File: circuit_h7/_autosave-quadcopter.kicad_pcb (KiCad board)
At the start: 4 copper layers, 37.5 x 37.5 mm, 108 parts, among them J1 Conn_01x04_Male, J10 Conn_01x01_Female, J11 Conn_01x04_Male, J12 Conn_01x04_Male, J13 Conn_01x01_Female, J14 Conn_01x01_Female, J16 Conn_01x01_Female, J17 Conn_01x01_Female, J18 USB_C_Receptacle_USB2.0, J19 Conn_01x08_Male, J2 Conn_01x01_Female, J21 Conn_01x01_Female, J22 Conn_01x01_Female, J23 Conn_01x01_Female, J24 Conn_01x01_Female, J25 Conn_01x01_Female, J26 Conn_01x01_Female, J28 Conn_01x01_Female, J29 Conn_01x01_Female, J3 Conn_01x01_Female, J30 Conn_01x01_Female, J31 Conn_01x01_Female, J32 Conn_01x01_Female, J33 Conn_01x01_Female, J37 Conn_01x01_Female, J4 Conn_01x01_Female, J40 Conn_01x01_Female, J41 Conn_01x01_Female, J42 Conn_01x01_Female, J43 Conn_01x01_Female, J44 Conn_01x01_Female, J45 Conn_01x01_Female, J47 Conn_01x01_Female, J48 Conn_01x01_Female, J49 Conn_01x01_Female, J5 Conn_Coaxial, J50 Conn_01x01_Female, J6 Conn_01x06_Male, J7 Conn_01x01_Female, J8 Conn_01x01_Female, J9 Conn_01x01_Female, SW1 SW_DIP_x01, U1 STM32H723VGH6, U2 ICM-42605, U3 DPS310, U4 3V3, U5 EUP3458 1.2A, 30V max input, 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, U6 2450FM07D0034T, U7 W25Q80DVUXIE TR (16M), U8 SX1281, U9 5v, 500mA, Y1 16M, Y2 52Mhz, 12pF

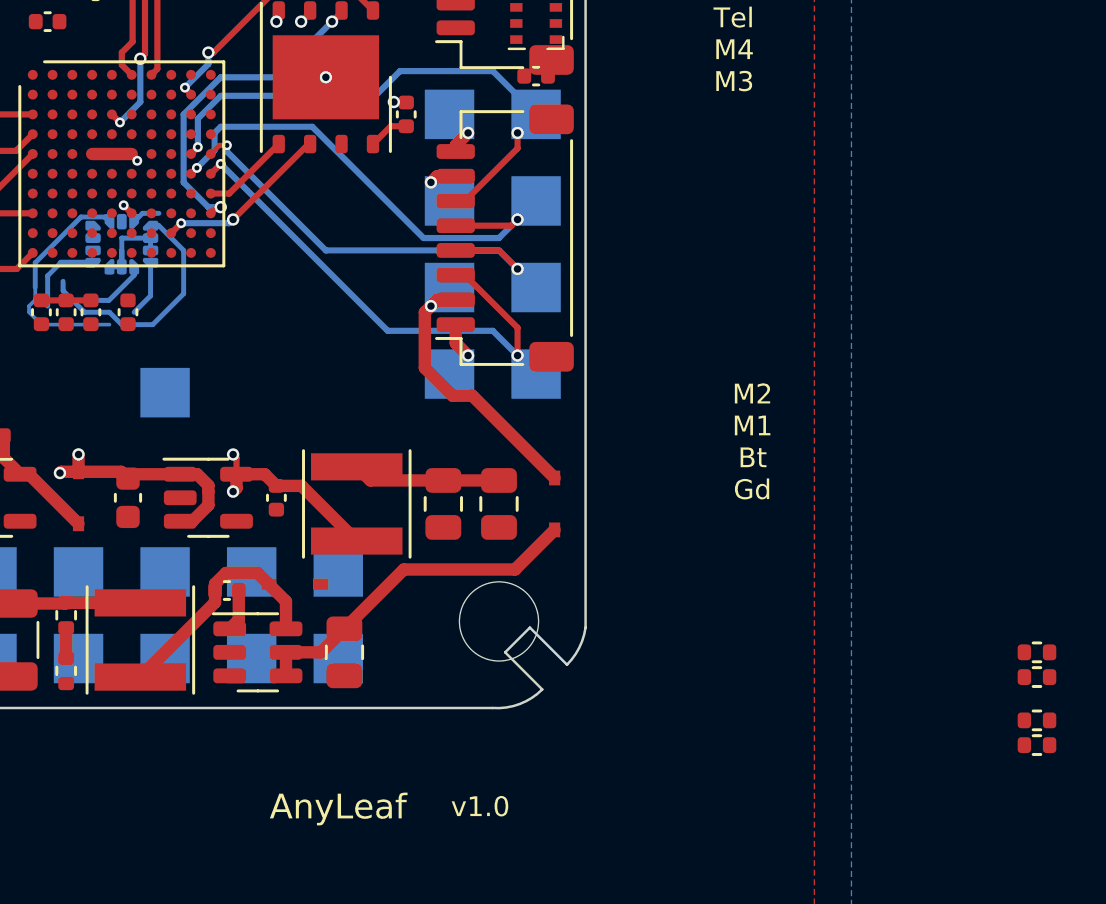
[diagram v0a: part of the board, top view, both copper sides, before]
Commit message: Started work on getting all 4 motors on same timer for H7 design
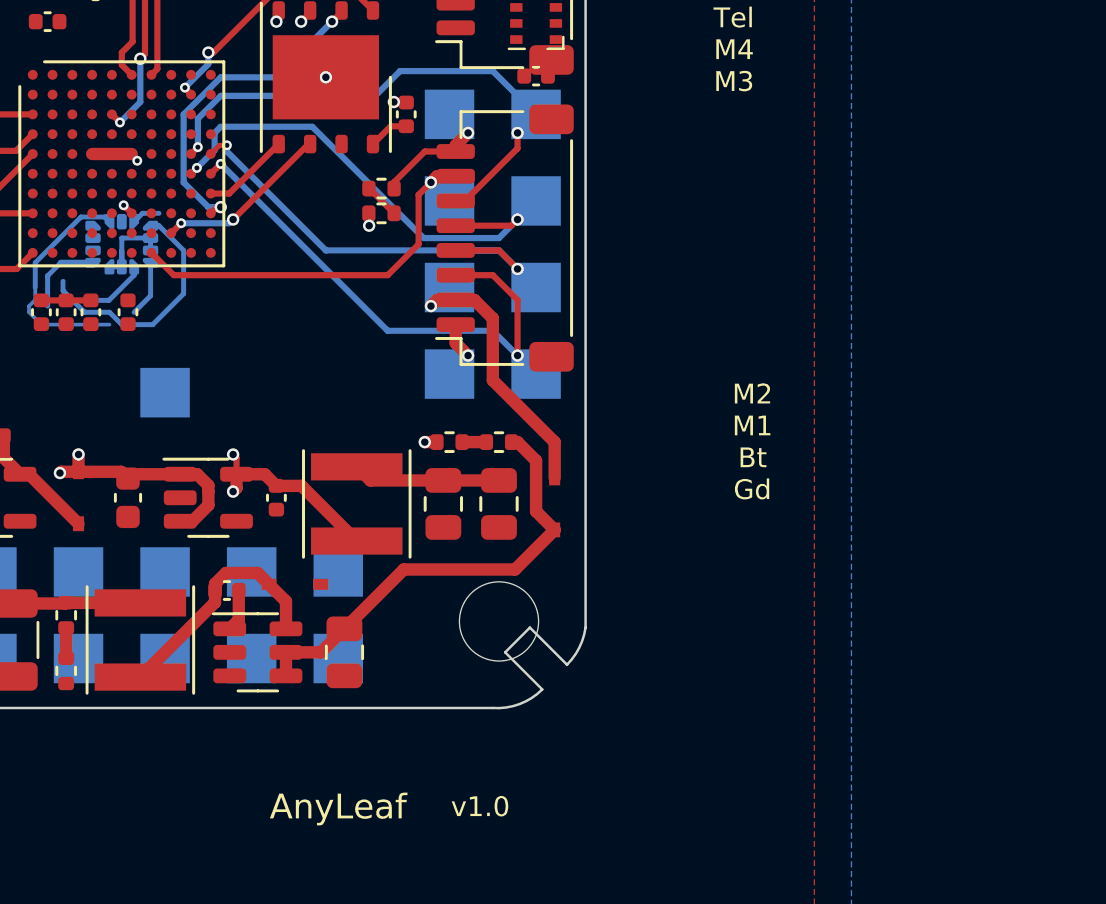
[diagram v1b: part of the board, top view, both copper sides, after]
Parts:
- moved R16 34.8 mm to (147.5, 85.2)
- moved R18 33.5 mm to (147.5, 86.2)
- moved R14 25.2 mm to (150.2, 95.5)
- moved R13 23.7 mm to (152.2, 95.5), turned to 0 degrees
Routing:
- net /UART3_RX: track 1.10 -> 15.5 mm
- net +BATT: track 13.9 -> 18.3 mm
- net /CURRENT: track 1.71 -> 4.97 mm
- net /CUR_DIV: track 0.00 -> 1.43 mm
- net GND: track 17.7 -> 18.6 mm, vias 8 -> 10
- net /BATT_DIV: track 0.00 -> 0.98 mm
- net /M1: track 20.3 -> 20.9 mm
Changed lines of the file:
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@@
   )
   (footprint "Resistor_SMD:R_0402_1005Metric" (layer "F.Cu")
-    (at 174 104)
+    (at 150.25 95.5)
     (descr "Resistor SMD 0402 (1005 Metric), square (rectangular) end terminal, IPC_7351 nominal, (Body size source: IPC-SM-782 page 72, https://www.pcb-3d.com/wordpress/wp-content/uploads/ipc-sm-782a_amendment_1_and_2.pdf), generated with kicad-footprint-generator")
     (tags "resistor")
@@
   )
   (footprint "Resistor_SMD:R_0402_1005Metric" (layer "F.Cu")
-    (at 174 107.75)
+    (at 147.5 85.25)
     (descr "Resistor SMD 0402 (1005 Metric), square (rectangular) end terminal, IPC_7351 nominal, (Body size source: IPC-SM-782 page 72, https://www.pcb-3d.com/wordpress/wp-content/uploads/ipc-sm-782a_amendment_1_and_2.pdf), generated with kicad-footprint-generator")
     (tags "resistor")
@@
   )
   (footprint "Resistor_SMD:R_0402_1005Metric" (layer "F.Cu")
-    (at 174 105 180)
+    (at 152.25 95.5)
     (descr "Resistor SMD 0402 (1005 Metric), square (rectangular) end terminal, IPC_7351 nominal, (Body size source: IPC-SM-782 page 72, https://www.pcb-3d.com/wordpress/wp-content/uploads/ipc-sm-782a_amendment_1_and_2.pdf), generated with kicad-footprint-generator")
     (tags "resistor")
@@
     (fp_line (start 0.525 -0.27) (end 0.525 0.27) (layer "F.Fab") (width 0.1))
     (fp_line (start -0.525 -0.27) (end 0.525 -0.27) (layer "F.Fab") (width 0.1))
-    (pad "1" smd roundrect locked (at -0.51 0 180) (size 0.54 0.64) (layers "F.Cu" "F.Paste" "F.Mask") (roundrect_rratio 0.25)
+    (pad "1" smd roundrect locked (at -0.51 0) (size 0.54 0.64) (layers "F.Cu" "F.Paste" "F.Mask") (roundrect_rratio 0.25)
       (net 57 "/BATT_DIV") (pintype "passive"))
-    (pad "2" smd roundrect locked (at 0.51 0 180) (size 0.54 0.64) (layers "F.Cu" "F.Paste" "F.Mask") (roundrect_rratio 0.25)
+    (pad "2" smd roundrect locked (at 0.51 0) (size 0.54 0.64) (layers "F.Cu" "F.Paste" "F.Mask") (roundrect_rratio 0.25)
       (net 15 "+BATT") (pintype "passive"))
     (model "${KICAD6_3DMODEL_DIR}/Resistor_SMD.3dshapes/R_0402_1005Metric.wrl"
@@
   )
   (footprint "Resistor_SMD:R_0402_1005Metric" (layer "F.Cu")
-    (at 174 106.75)
+    (at 147.5 86.25)
     (descr "Resistor SMD 0402 (1005 Metric), square (rectangular) end terminal, IPC_7351 nominal, (Body size source: IPC-SM-782 page 72, https://www.pcb-3d.com/wordpress/wp-content/uploads/ipc-sm-782a_amendment_1_and_2.pdf), generated with kicad-footprint-generator")
     (tags "resistor")
@@
   (segment (start 148.02 81.77) (end 148 81.75) (width 0.25) (layer "F.Cu") (net 8))
   (segment (start 122.75 82.25) (end 123.5 83) (width 0.25) (layer "F.Cu") (net 8))
+  (segment (start 146.99 86.74) (end 147 86.75) (width 0.25) (layer "F.Cu") (net 8))
   (segment (start 123.5 83) (end 123.5 83.5) (width 0.25) (layer "F.Cu") (net 8))
   (segment (start 122.075 82.25) (end 122.75 82.25) (width 0.25) (layer "F.Cu") (net 8))
+  (segment (start 146.99 86.25) (end 146.99 86.74) (width 0.25) (layer "F.Cu") (net 8))
+  (segment (start 149.74 95.5) (end 149.25 95.5) (width 0.5) (layer "F.Cu") (net 8))
   (segment (start 137.1875 72.75) (end 137.0525 72.885) (width 0.2) (layer "F.Cu") (net 8))
   (segment (start 139.125 74) (end 139.125 74.5) (width 0.25) (layer "F.Cu") (net 8))
@@
   (via (at 145.25 80.75) (size 0.5) (drill 0.3) (layers "F.Cu" "B.Cu") (net 8))
   (via (at 137.625 84.125) (size 0.4) (drill 0.2) (layers "F.Cu" "B.Cu") (net 8))
+  (via (at 147 86.75) (size 0.5) (drill 0.3) (layers "F.Cu" "B.Cu") (net 8))
   (via (at 143.25 78.5) (size 0.5) (drill 0.3) (layers "F.Cu" "B.Cu") (net 8))
   (via (at 137.25 73.75) (size 0.5) (drill 0.3) (layers "F.Cu" "B.Cu") (net 8))
@@
   (via (at 148 81.75) (size 0.5) (drill 0.3) (layers "F.Cu" "B.Cu") (net 8))
   (via (at 123.5 83.5) (size 0.5) (drill 0.3) (layers "F.Cu" "B.Cu") (net 8))
+  (via (at 149.25 95.5) (size 0.5) (drill 0.3) (layers "F.Cu" "B.Cu") (net 8))
   (segment (start 137 88.4125) (end 136.5 88.4125) (width 0.2) (layer "B.Cu") (net 8))
   (segment (start 137 87.75) (end 137 88.4125) (width 0.2) (layer "B.Cu") (net 8))
@@
   (segment (start 135.439438 100.689438) (end 135.25 100.5) (width 0.25) (layer "B.Cu") (net 14))
   (segment (start 152.899521 100.650479) (end 154.5 99.05) (width 0.5) (layer "F.Cu") (net 15))
+  (segment (start 153.75 96.25) (end 153.75 98.3) (width 0.5) (layer "F.Cu") (net 15))
+  (segment (start 152.76 95.5) (end 153 95.5) (width 0.5) (layer "F.Cu") (net 15))
+  (segment (start 153.75 98.3) (end 154.5 99.05) (width 0.5) (layer "F.Cu") (net 15))
   (segment (start 148.399521 100.650479) (end 152.899521 100.650479) (width 0.5) (layer "F.Cu") (net 15))
   (segment (start 146 103.05) (end 145.05 104) (width 0.5) (layer "F.Cu") (net 15))
   (segment (start 145.05 104) (end 143.6375 104) (width 0.5) (layer "F.Cu") (net 15))
+  (segment (start 153 95.5) (end 153.75 96.25) (width 0.5) (layer "F.Cu") (net 15))
   (segment (start 143.6375 104) (end 143.6375 104.95) (width 0.5) (layer "F.Cu") (net 15))
   (segment (start 146 103.05) (end 148.399521 100.650479) (width 0.5) (layer "F.Cu") (net 15))
@@
   (segment (start 132.725489 83.724511) (end 130.474511 83.724511) (width 0.25) (layer "F.Cu") (net 22))
   (segment (start 150.5 83.75) (end 150.5 83.5) (width 0.5) (layer "F.Cu") (net 23))
+  (segment (start 149.25 83.75) (end 148.01 84.99) (width 0.25) (layer "F.Cu") (net 23))
   (segment (start 150.5 83.5) (end 151 83) (width 0.5) (layer "F.Cu") (net 23))
+  (segment (start 148.01 84.99) (end 148.01 85.25) (width 0.25) (layer "F.Cu") (net 23))
+  (segment (start 150.5 83.75) (end 149.25 83.75) (width 0.25) (layer "F.Cu") (net 23))
   (via (at 151 83) (size 0.5) (drill 0.3) (layers "F.Cu" "B.Cu") (net 23))
   (segment (start 150 82.25) (end 150 83) (width 0.2) (layer "B.Cu") (net 23))
-  (segment (start 151.175 93.625) (end 150.375 93.625) (width 0.5) (layer "F.Cu") (net 26))
-  (segment (start 149.25 90.25) (end 149.25 92.5) (width 0.5) (layer "F.Cu") (net 26))
-  (segment (start 149.5 90) (end 149.25 90.25) (width 0.5) (layer "F.Cu") (net 26))
-  (segment (start 149.25 92.5) (end 150.375 93.625) (width 0.5) (layer "F.Cu") (net 26))
+  (segment (start 154.5 95.5) (end 152 93) (width 0.5) (layer "F.Cu") (net 26))
+  (segment (start 152 90.5) (end 151.25 89.75) (width 0.5) (layer "F.Cu") (net 26))
+  (segment (start 152 93) (end 152 90.5) (width 0.5) (layer "F.Cu") (net 26))
   (segment (start 150.5 89.75) (end 149.75 89.75) (width 0.5) (layer "F.Cu") (net 26))
-  (segment (start 154.5 96.95) (end 151.175 93.625) (width 0.5) (layer "F.Cu") (net 26))
+  (segment (start 154.5 96.95) (end 154.5 95.5) (width 0.5) (layer "F.Cu") (net 26))
+  (segment (start 151.25 89.75) (end 150.5 89.75) (width 0.5) (layer "F.Cu") (net 26))
   (segment (start 149.75 89.75) (end 149.5 90) (width 0.5) (layer "F.Cu") (net 26))
   (via (at 149.5 90) (size 0.5) (drill 0.3) (layers "F.Cu" "B.Cu") (net 26))
@@
   (via (at 120.75 81.5) (size 0.5) (drill 0.3) (layers "F.Cu" "B.Cu") (net 32))
   (segment (start 150.5 84.75) (end 149.75 84.75) (width 0.5) (layer "F.Cu") (net 34))
+  (segment (start 149 87.5) (end 149 85.5) (width 0.25) (layer "F.Cu") (net 34))
   (segment (start 149.75 84.75) (end 149.5 85) (width 0.5) (layer "F.Cu") (net 34))
+  (segment (start 138.2 87.85) (end 139.1 88.75) (width 0.25) (layer "F.Cu") (net 34))
+  (segment (start 147.75 88.75) (end 149 87.5) (width 0.25) (layer "F.Cu") (net 34))
+  (segment (start 149 85.5) (end 149.5 85) (width 0.25) (layer "F.Cu") (net 34))
+  (segment (start 139.1 88.75) (end 147.75 88.75) (width 0.25) (layer "F.Cu") (net 34))
   (via (at 149.5 85) (size 0.5) (drill 0.3) (layers "F.Cu" "B.Cu") (net 34))
   (segment (start 126 101.1875) (end 126 102.7) (width 0.5) (layer "F.Cu") (net 37))
@@
   (segment (start 141.25 83.75) (end 141.25 83.5) (width 0.25) (layer "B.Cu") (net 53))
   (segment (start 145.25 87.75) (end 152.25 87.75) (width 0.25) (layer "B.Cu") (net 53))
-  (segment (start 150.875361 88.75) (end 153 90.874639) (width 0.25) (layer "F.Cu") (net 54))
-  (segment (start 153 90.874639) (end 153 92) (width 0.25) (layer "F.Cu") (net 54))
-  (segment (start 150.5 88.75) (end 150.875361 88.75) (width 0.25) (layer "F.Cu") (net 54))
+  (segment (start 150.5 88.75) (end 152 88.75) (width 0.25) (layer "F.Cu") (net 54))
+  (segment (start 153 89.75) (end 153 92) (width 0.25) (layer "F.Cu") (net 54))
+  (segment (start 152 88.75) (end 153 89.75) (width 0.25) (layer "F.Cu") (net 54))
   (segment (start 140.6 84.65) (end 141 84.25) (width 0.25) (layer "F.Cu") (net 54))
   (via (at 141 84.25) (size 0.4) (drill 0.2) (layers "F.Cu" "B.Cu") (net 54))
@@
   (segment (start 141 82.75) (end 144.700978 82.75) (width 0.25) (layer "B.Cu") (net 56))
   (segment (start 140.75 83.7) (end 140.75 83) (width 0.25) (layer "B.Cu") (net 56))
+  (segment (start 151.74 95.5) (end 150.76 95.5) (width 0.5) (layer "F.Cu") (net 57))
+  (segment (start 146.99 85.25) (end 147.01 85.25) (width 0.25) (layer "F.Cu") (net 58))
+  (segment (start 147.01 85.25) (end 148.01 86.25) (width 0.25) (layer "F.Cu") (net 58))
   (segment (start 135.119093 71.8125) (end 134.207082 72.724511) (width 0.25) (layer "F.Cu") (net 59))
   (segment (start 131.712011 72.724511) (end 130.8375 71.85) (width 0.25) (layer "F.Cu") (net 59))

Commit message: Set up ADC measurements
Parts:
- added J15: Conn_01x01_Female, TestPoint:TestPoint_Pad_2.0x2.0mm, B.Cu at (138.8, 97.2)
- moved J32 5.13 mm to (135.2, 97.2)
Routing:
- net /USB_DP: track 0.00 -> 21.1 mm, vias 0 -> 2
- net /USB_DN: track 0.00 -> 20.0 mm, vias 0 -> 2
- net /IMU_pwr: track 13.9 -> 33.3 mm
- net /BOOT0: track 0.00 -> 14.2 mm, vias 0 -> 2
- net /CUR_DIV: track 1.43 -> 13.6 mm, vias 0 -> 2
- net GND: track 18.6 -> 22.4 mm, vias 10 -> 15
- net +5V: track 9.57 -> 10.3 mm
- net +3V3: vias 3 -> 5
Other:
- board text added: "I2C"
